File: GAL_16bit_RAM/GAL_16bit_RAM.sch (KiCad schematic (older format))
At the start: 8 parts, among them CN1 HDR-1X12-SIP-100, CN2 HDR-1X12-SIP-100, CN3 HDR-1X12-SIP-100, IC1 74574N, U1 GAL16V8, U2 AS7C4098-15TC

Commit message: fixed net label typo
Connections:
- net 1.2 renamed LB*
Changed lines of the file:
@@
 Text Label 6250 5400 0    47   ~ 0
 UB*
-Text Label 6250 5500 0    70   ~ 0
-1.2
+Text Label 6250 5500 0    47   ~ 0
+LB*
 Entry Wire Line
 	4700 2350 4800 2450
@@
 AR Path="/619031E1/61AF553A" Ref="IC?"  Part="1"
 F 0 "IC1" H 5800 3575 59  0000 L BNN
-F 1 "74574N" H 5800 2250 59  0001 L BNN
+F 1 "74574N" H 5800 2250 59  0000 L BNN
 F 2 "GAL_16bit_RAM:DIL20" H 6100 2950 50  0001 C CNN
 F 3 "" H 6100 2950 50  0001 C CNN
@@
 Wire Wire Line
 	4600 6200 4400 6200
-Wire Bus Line
-	6200 1700 7000 1700
-Wire Bus Line
-	4700 4100 7100 4100
-Wire Bus Line
-	2850 5000 2850 7500
-Wire Bus Line
-	7100 2900 7100 4100
-Wire Bus Line
-	4700 1700 4700 4100
-Wire Bus Line
-	2100 3900 2100 7400
-Wire Bus Line
-	7000 1700 7000 3500
-Wire Bus Line
-	10100 1700 10100 3500
 $Comp
 L power:VCC #PWR01
@@
 	1    0    0    -1
 $EndComp
+Wire Bus Line
+	6200 1700 7000 1700
+Wire Bus Line
+	4700 4100 7100 4100
+Wire Bus Line
+	2850 5000 2850 7500
+Wire Bus Line
+	7100 2900 7100 4100
+Wire Bus Line
+	4700 1700 4700 4100
+Wire Bus Line
+	2100 3900 2100 7400
+Wire Bus Line
+	7000 1700 7000 3500
+Wire Bus Line
+	10100 1700 10100 3500
 $EndSCHEMATC

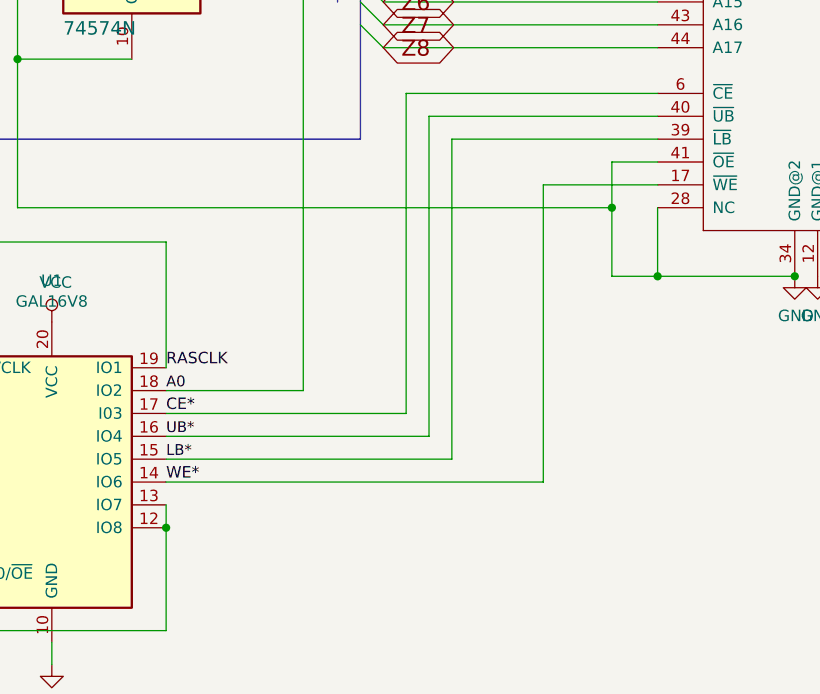
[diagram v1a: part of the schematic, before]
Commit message: Added option to control OE
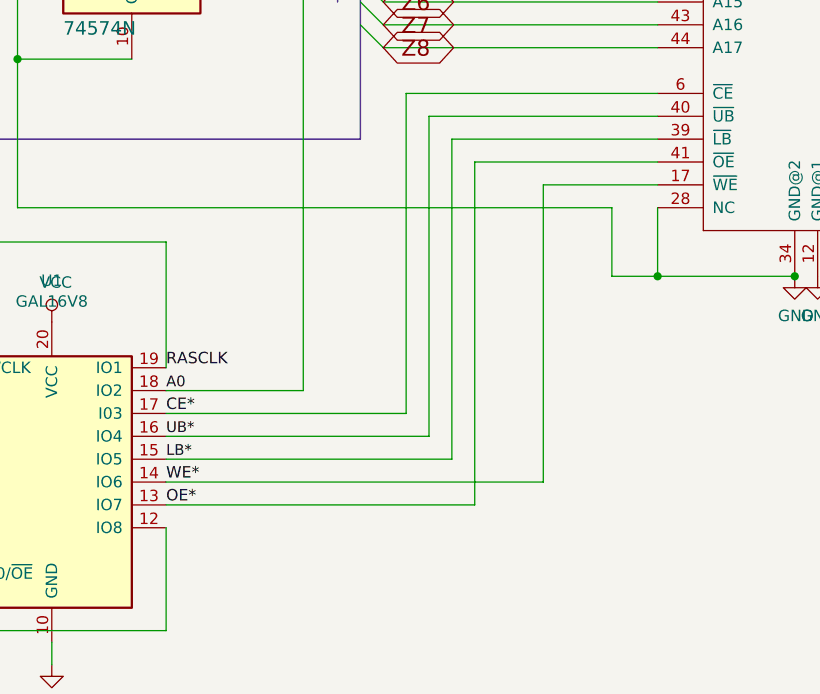
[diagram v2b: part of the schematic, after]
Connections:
- net GND: no longer U2.41 (~OE)
- net at R1.1, U1.11 (I10/~OE~), U1.12 (IO8)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: no longer U1.13 (IO7)
- new net OE*: U1.13 (IO7), U2.41 (~OE)
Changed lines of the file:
@@
 A8
-Wire Wire Line
-	8400 4200 8200 4200
-Wire Wire Line
-	8200 4200 8200 4400
 Wire Wire Line
 	8200 4700 8400 4700
@@
 Wire Wire Line
 	5600 4400 8200 4400
-Connection ~ 8200 4400
 Wire Wire Line
 	8200 4400 8200 4700
@@
 Wire Wire Line
 	6250 6250 6250 5800
-Wire Wire Line
-	6250 5700 6250 5800
-Connection ~ 6250 5800
 Wire Wire Line
 	9000 1700 8900 1700
@@
 	1    0    0    -1
 $EndComp
+Wire Wire Line
+	8400 4200 7600 4200
+Wire Wire Line
+	7600 4200 7600 5700
+Wire Wire Line
+	7600 5700 6250 5700
 Wire Bus Line
 	6200 1700 7000 1700
@@
 Wire Bus Line
 	10100 1700 10100 3500
+Text Label 6250 5700 0    50   ~ 0
+OE*
 $EndSCHEMATC

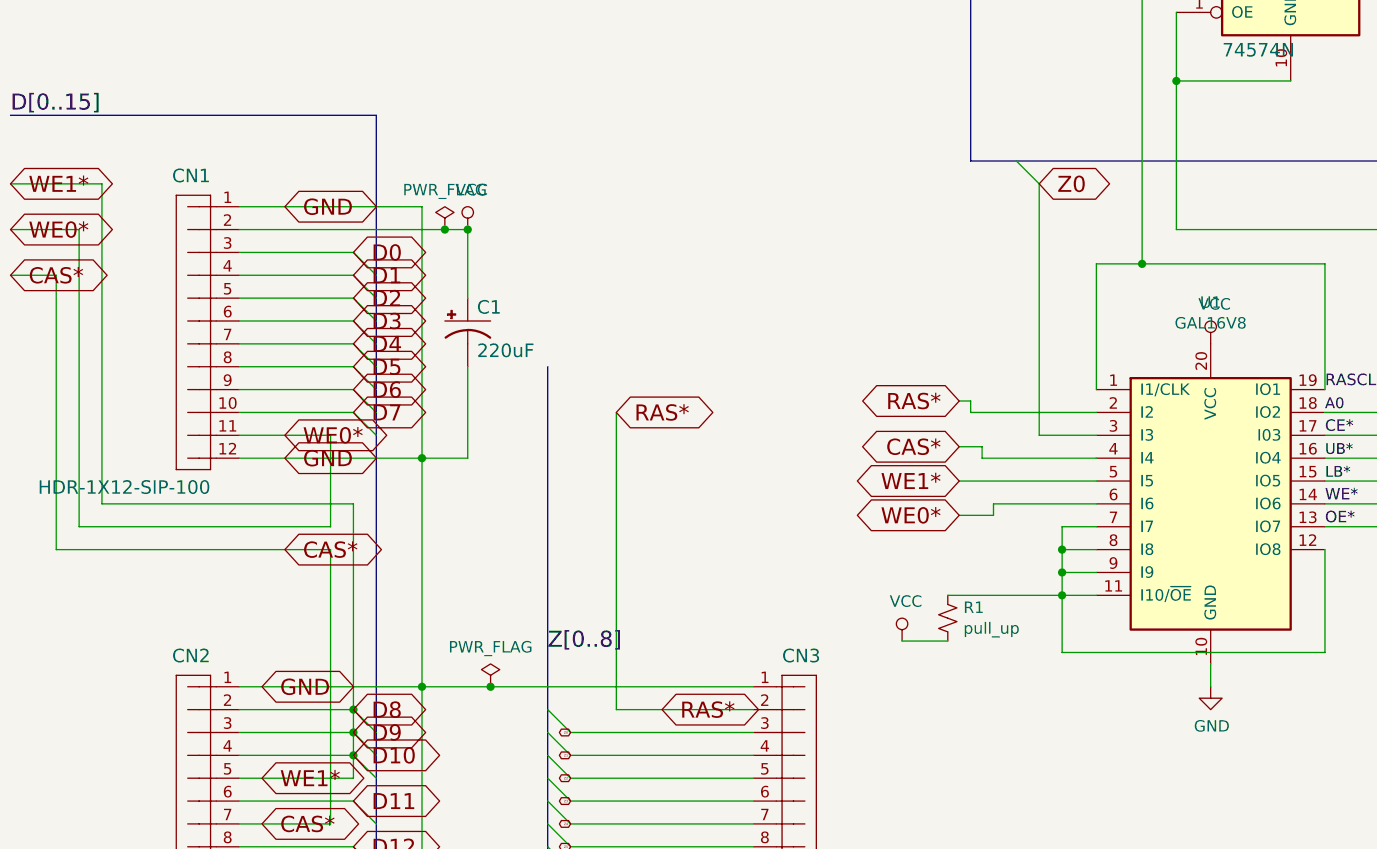
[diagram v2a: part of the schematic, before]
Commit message: fixed motherboard connector designations
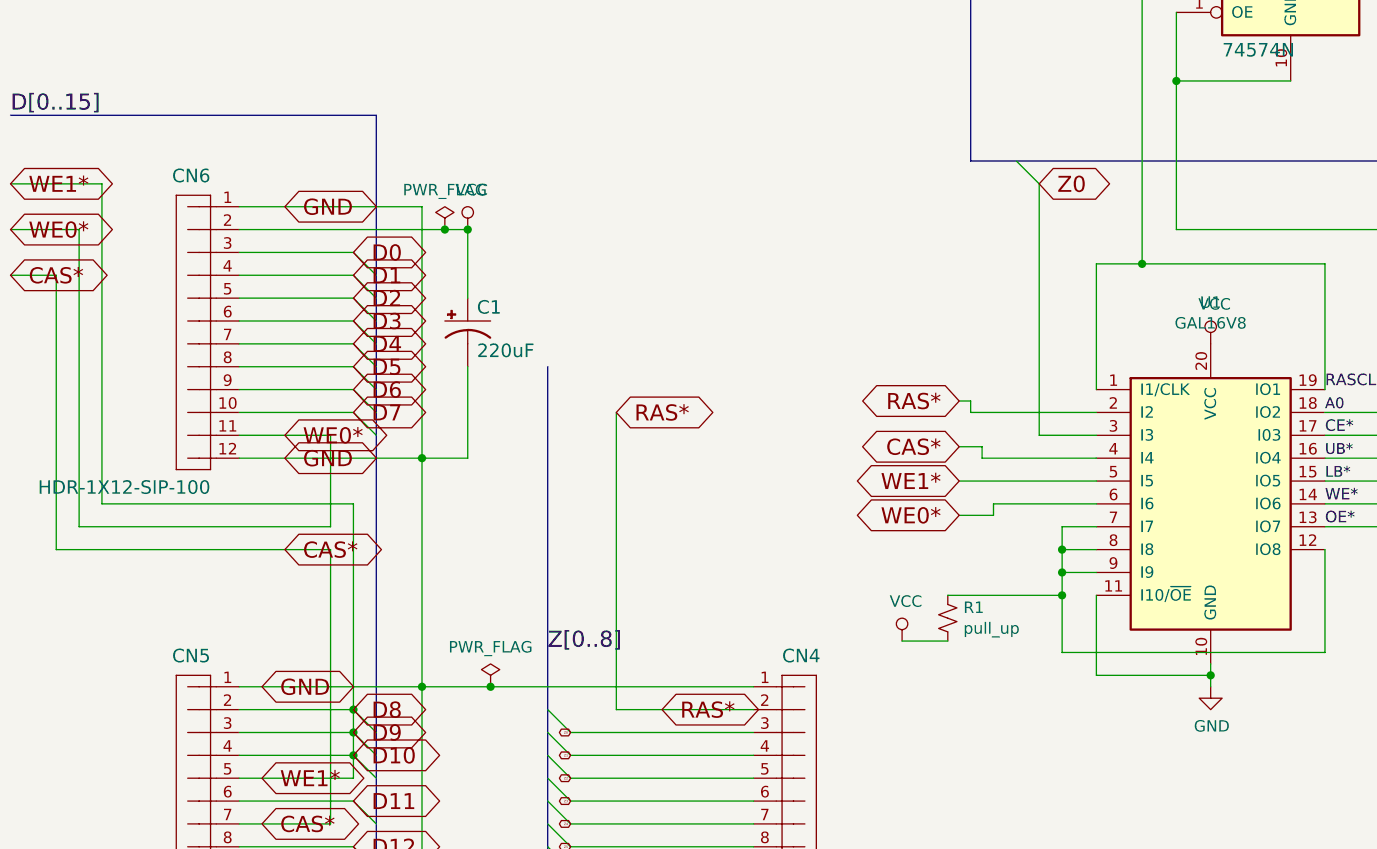
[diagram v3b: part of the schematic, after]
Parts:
- renumbered CN3 to CN4, CN2 to CN5, CN1 to CN6
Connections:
- net GND: now also U1.11 (I10/~OE~)
- net at R1.1, U1.12 (IO8), U1.7 (I7)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: no longer U1.11 (I10/~OE~)
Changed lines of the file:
@@
 	2850 7300 2950 7400
 $Comp
-L GAL_16bit_RAM-eagle-import:HDR-1X12-SIP-100 CN1
+L GAL_16bit_RAM-eagle-import:HDR-1X12-SIP-100 CN6
 U 1 1 61ABE9F1
 P 1300 4800
-AR Path="/61ABE9F1" Ref="CN1"  Part="1"
+AR Path="/61ABE9F1" Ref="CN6"  Part="1"
 AR Path="/61903186/61ABE9F1" Ref="CN?"  Part="1"
-F 0 "CN1" H 1225 5400 59  0000 L BNN
+F 0 "CN6" H 1225 5400 59  0000 L BNN
 F 1 "HDR-1X12-SIP-100" H 1225 4037 59  0000 L BNN
 F 2 "GAL_16bit_RAM:SIP-100-12V" H 1300 4800 50  0001 C CNN
@@
 $EndComp
 $Comp
-L GAL_16bit_RAM-eagle-import:HDR-1X12-SIP-100 CN2
+L GAL_16bit_RAM-eagle-import:HDR-1X12-SIP-100 CN5
 U 1 1 61ABE9F7
 P 1300 6900
-AR Path="/61ABE9F7" Ref="CN2"  Part="1"
+AR Path="/61ABE9F7" Ref="CN5"  Part="1"
 AR Path="/61903186/61ABE9F7" Ref="CN?"  Part="1"
-F 0 "CN2" H 1225 7500 59  0000 L BNN
+F 0 "CN5" H 1225 7500 59  0000 L BNN
 F 1 "HDR-1X12-SIP-100" H 1225 6137 59  0000 L BNN
 F 2 "GAL_16bit_RAM:SIP-100-12V" H 1300 6900 50  0001 C CNN
@@
 $EndComp
 $Comp
-L GAL_16bit_RAM-eagle-import:HDR-1X12-SIP-100 CN3
+L GAL_16bit_RAM-eagle-import:HDR-1X12-SIP-100 CN4
 U 1 1 61ABE9FD
 P 3950 6900
-AR Path="/61ABE9FD" Ref="CN3"  Part="1"
+AR Path="/61ABE9FD" Ref="CN4"  Part="1"
 AR Path="/61903186/61ABE9FD" Ref="CN?"  Part="1"
-F 0 "CN3" H 3875 7500 59  0000 L BNN
+F 0 "CN4" H 3875 7500 59  0000 L BNN
 F 1 "HDR-1X12-SIP-100" H 3875 6137 59  0000 L BNN
 F 2 "GAL_16bit_RAM:SIP-100-12V" H 3950 6900 50  0001 C CNN
@@
 Connection ~ 5100 5800
 Wire Wire Line
-	5250 6000 5100 6000
-Wire Wire Line
 	5100 6000 5100 5900
 Connection ~ 5100 5900
@@
 $EndComp
 Wire Wire Line
-	5750 6300 5750 6400
+	5750 6300 5750 6350
 $Comp
 L power:GND #PWR0107
@@
 Wire Wire Line
 	7600 5700 6250 5700
-Wire Bus Line
-	6200 1700 7000 1700
-Wire Bus Line
-	4700 4100 7100 4100
-Wire Bus Line
-	2850 5000 2850 7500
-Wire Bus Line
-	7100 2900 7100 4100
-Wire Bus Line
-	4700 1700 4700 4100
-Wire Bus Line
-	2100 3900 2100 7400
-Wire Bus Line
-	7000 1700 7000 3500
-Wire Bus Line
-	10100 1700 10100 3500
 Text Label 6250 5700 0    50   ~ 0
 OE*
+Wire Wire Line
+	5250 6000 5250 6350
+Wire Wire Line
+	5250 6350 5750 6350
+Wire Bus Line
+	6200 1700 7000 1700
+Wire Bus Line
+	4700 4100 7100 4100
+Wire Bus Line
+	2850 5000 2850 7500
+Wire Bus Line
+	7100 2900 7100 4100
+Wire Bus Line
+	4700 1700 4700 4100
+Wire Bus Line
+	2100 3900 2100 7400
+Wire Bus Line
+	7000 1700 7000 3500
+Wire Bus Line
+	10100 1700 10100 3500
+Connection ~ 5750 6350
+Wire Wire Line
+	5750 6350 5750 6400
 $EndSCHEMATC
